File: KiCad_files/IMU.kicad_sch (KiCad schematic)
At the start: 12 parts, among them U13 BNO085

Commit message: update
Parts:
- removed R19: DNI, Resistor_SMD:R_0805_2012Metric_Pad1.20x1.40mm_HandSolder, symbol Device:R
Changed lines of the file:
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@@
 	(text "pin17 can be used to select lower bit of i2c slave address, no idea what that means"
 		(exclude_from_sim no)
-		(at 250.444 60.96 0)
+		(at 248.158 29.21 0)
 		(effects
 			(font
@@
 	)
 	(junction
-		(at 102.87 52.07)
-		(diameter 0)
-		(color 0 0 0 0)
-	)
-	(junction
 		(at 114.3 92.71)
 		(diameter 0)
@@
 	)
 	(junction
-		(at 154.94 52.07)
-		(diameter 0)
-		(color 0 0 0 0)
-	)
-	(junction
 		(at 123.19 35.56)
 		(diameter 0)
@@
 	(wire
 		(pts
-			(xy 152.4 52.07) (xy 154.94 52.07)
-		)
-		(stroke
-			(width 0)
-			(type default)
-		)
-	)
-	(wire
-		(pts
 			(xy 36.83 99.06) (xy 46.99 99.06)
 		)
@@
 	(wire
 		(pts
-			(xy 102.87 52.07) (xy 102.87 60.96)
+			(xy 102.87 27.94) (xy 102.87 60.96)
 		)
 		(stroke
@@
 	(wire
 		(pts
-			(xy 102.87 52.07) (xy 144.78 52.07)
-		)
-		(stroke
-			(width 0)
-			(type default)
-		)
-	)
-	(wire
-		(pts
 			(xy 119.38 92.71) (xy 114.3 92.71)
 		)
@@
 		(pts
 			(xy 190.5 87.63) (xy 195.58 87.63)
-		)
-		(stroke
-			(width 0)
-			(type default)
-		)
-	)
-	(wire
-		(pts
-			(xy 102.87 27.94) (xy 102.87 52.07)
 		)
 		(stroke
@@
 					(unit 1)
 				)
-			)
-		)
-	)
-	(symbol
-		(lib_id "Device:R")
-		(at 148.59 52.07 90)
-		(unit 1)
-		(exclude_from_sim no)
-		(in_bom yes)
-		(on_board yes)
-		(dnp no)
-		(fields_autoplaced yes)
-		(property "Reference" "R19"
-			(at 148.59 45.72 90)
-			(effects
-				(font
-					(size 1.27 1.27)
-				)
-			)
-		)
-		(property "Value" "DNI"
-			(at 148.59 48.26 90)
-			(effects
-				(font
-					(size 1.27 1.27)
-				)
-			)
-		)
-		(property "Footprint" "Resistor_SMD:R_0805_2012Metric_Pad1.20x1.40mm_HandSolder"
-			(at 148.59 53.848 90)
-			(effects
-				(font
-					(size 1.27 1.27)
-				)
-				(hide yes)
-			)
-		)
-		(property "Datasheet" "~"
-			(at 148.59 52.07 0)
-			(effects
-				(font
-					(size 1.27 1.27)
-				)
-				(hide yes)
-			)
-		)
-		(property "Description" "Resistor"
-			(at 148.59 52.07 0)
-			(effects
-				(font
-					(size 1.27 1.27)
-				)
-				(hide yes)
-			)
-		)
-		(property "MNF PART NUMBER" ""
-			(at 148.59 52.07 90)
-			(effects
-				(font
-					(size 1.27 1.27)
-				)
-				(hide yes)
-			)
-		)
-		(pin "1"
-		)
-		(pin "2"
-		)
-		(instances
-			(project ""
-				(path "/186d5500-054c-4b47-a89c-85f6ce2abe33/1d098c74-ef64-49cb-a95a-ee89cc8acd66"
-					(reference "R19")
-					(unit 1)
-				)

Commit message: i2c
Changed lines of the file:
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@@
 	)
 	(hierarchical_label "HOST_SDA"
-		(shape input)
+		(shape bidirectional)
 		(at 29.21 132.08 180)
 		(effects

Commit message: välipusku
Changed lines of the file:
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@@
 	)
 	(hierarchical_label "HOST_INTN"
-		(shape input)
+		(shape output)
 		(at 29.21 142.24 180)
 		(effects

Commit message: update
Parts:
- C22, C23, C24: DigiKey (none) -> 720-1754-1-ND
- R16, R23: value 10K -> 10k; DigiKey (none) -> 541-10.0KCCT-ND
- R17, R18, R21, R22: value 2.2K -> 2.2k; DigiKey (none) -> 311-2.20KCRCT-ND
- U13: DigiKey (none) -> 1888-1006-1-ND
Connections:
- net +3.3V: now also R23.2; no longer R23.1
- net BNO_CLKSFI0: no longer names the net of U13.10 (CLKSEL0)
- net BNO_CLKSFI0: now also R23.1; no longer R23.2
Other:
- moved on the sheet: C24, R16, R17, R18, R23

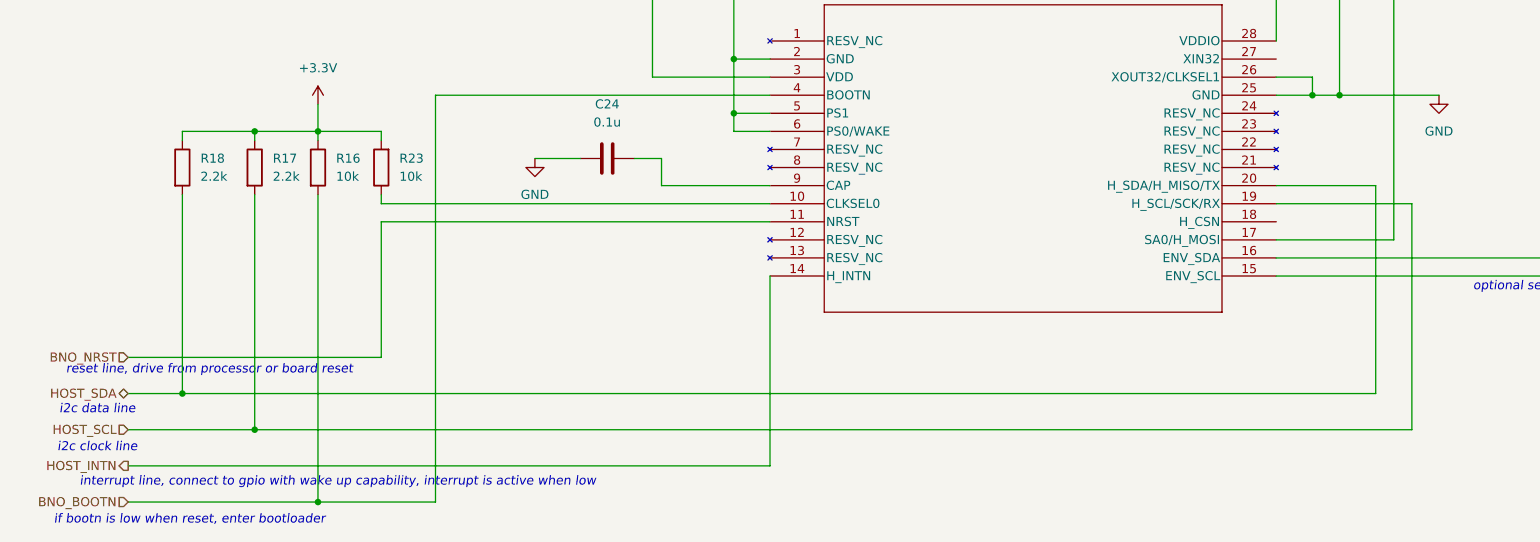
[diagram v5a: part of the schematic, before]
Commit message: piuhat vedetty mculla ja i2c pullupit mculle
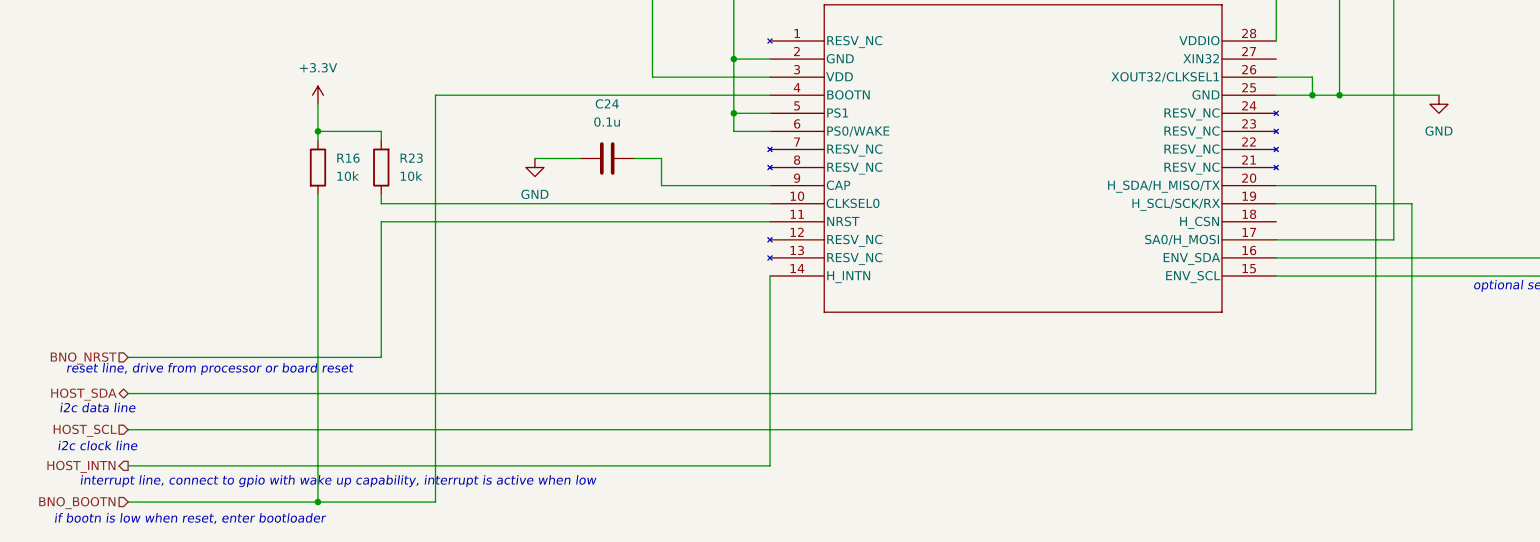
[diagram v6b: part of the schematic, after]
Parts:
- removed R17, R18: 2.2k, Resistor_SMD:R_0805_2012Metric_Pad1.20x1.40mm_HandSolder, symbol Device:R

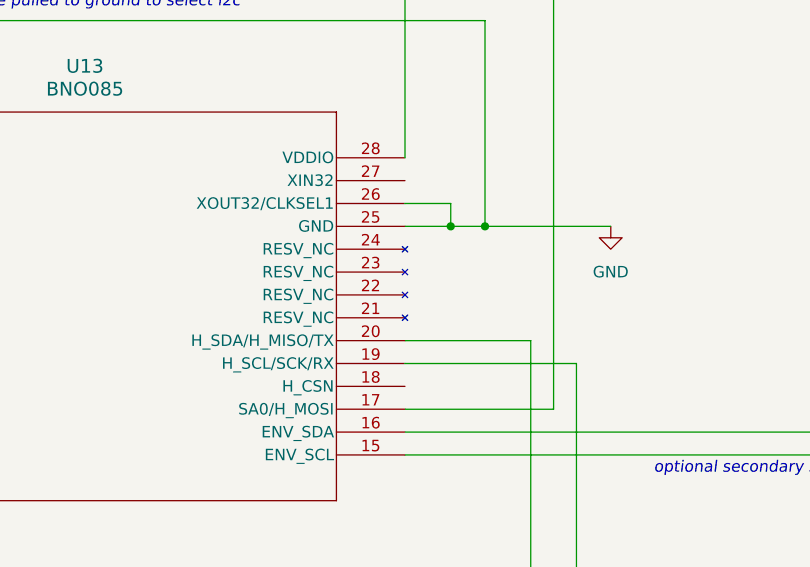
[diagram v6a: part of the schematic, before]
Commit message: ERC hiljennetty
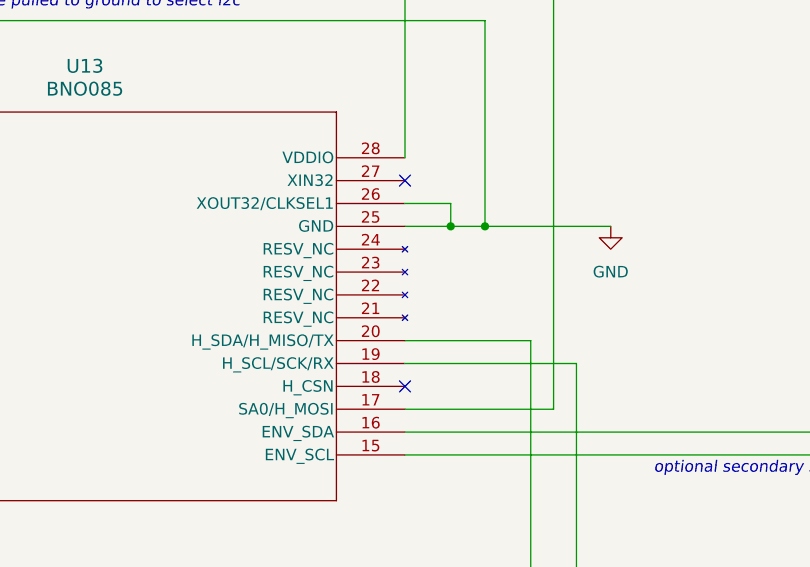
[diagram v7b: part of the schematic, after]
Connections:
- no-connect marks 0 -> 2
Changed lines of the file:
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@@
 		(color 0 0 0 0)
+	)
+	(no_connect
+		(at 190.5 107.95)
+	)
+	(no_connect
+		(at 190.5 85.09)
 	)
 	(wire
@@
 			(at 119.38 82.55 0)
 			(effects
-				(font
-					(size 1.27 1.27)
-				)
-				(hide yes)
-			)
-		)
-		(property "MNF PART NUMBER" ""
-			(at 119.38 82.55 0)
-			(effects
-				(font
-					(size 1.27 1.27)
-				)
-				(hide yes)
-			)
-		)
-		(property "Sim.Type" ""
-			(at 119.38 82.55 0)
-			(effects
